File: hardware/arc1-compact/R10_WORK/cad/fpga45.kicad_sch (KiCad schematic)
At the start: 109 parts, among them J9 45F JTAG, U26 LFE5U-45F-6BG381C, U27 iso FPGA45_SCK_B, U28 iso FPGA45_MOSI, U29 iso FPGA45_SS_N, X1 125MHz, X2 25MHz

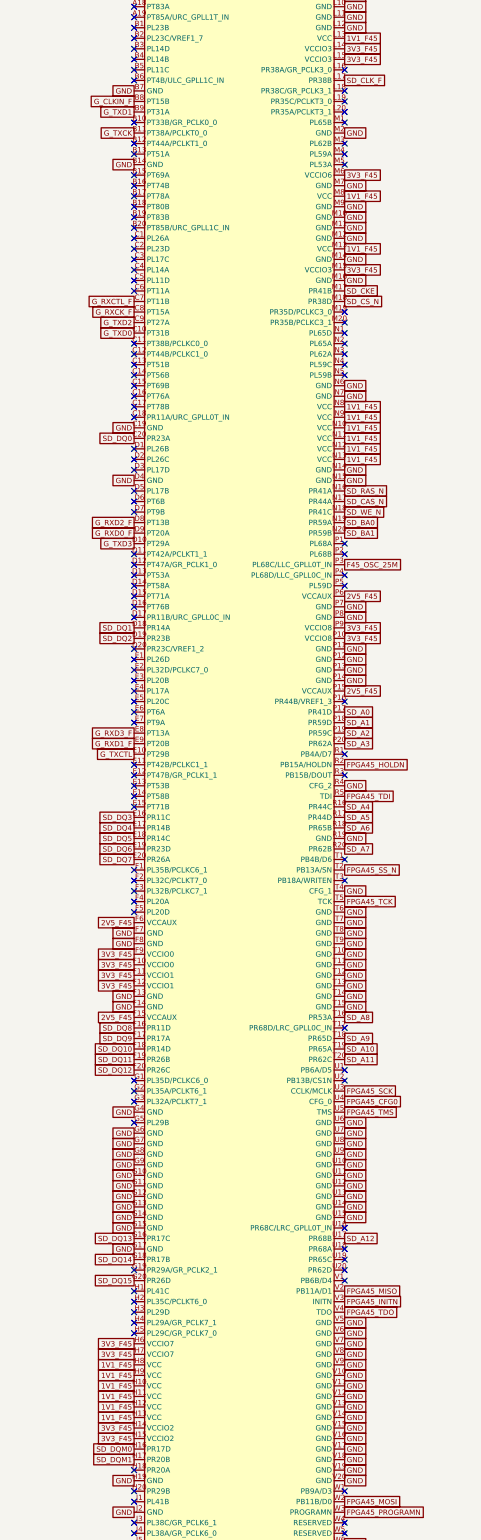
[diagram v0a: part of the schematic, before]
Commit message: R10 schematic: SDRAM net rename (collision with microSD clock found by crosscheck), 12F config buffers on 3V3_F12, crosscheck_r10 (A-H) PASS, every-pin review tables
Co-Authored-By: Claude Opus 5.5 <noreply@anthropic.com>
Claude-Session: https://claude.ai/code/session_01UkiuLdbjDvK75uDzAPKsGs
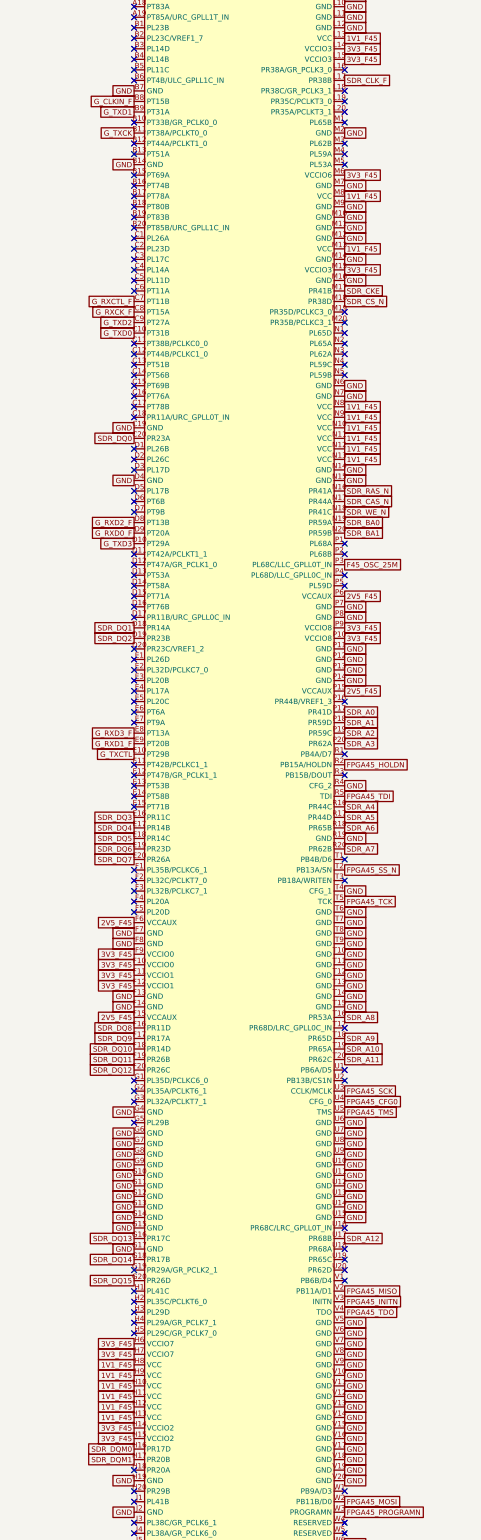
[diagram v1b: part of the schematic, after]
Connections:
- net SD_A0 renamed SDR_A0
- net SD_A1 renamed SDR_A1
- net SD_A10 renamed SDR_A10
- net SD_A11 renamed SDR_A11
- net SD_A12 renamed SDR_A12
- net SD_A2 renamed SDR_A2
- net SD_A3 renamed SDR_A3
- net SD_A4 renamed SDR_A4
- net SD_A5 renamed SDR_A5
- net SD_A6 renamed SDR_A6
- net SD_A7 renamed SDR_A7
- net SD_A8 renamed SDR_A8
- net SD_A9 renamed SDR_A9
- net SD_BA0 renamed SDR_BA0
- net SD_BA1 renamed SDR_BA1
- net SD_CAS_N renamed SDR_CAS_N
- net SD_CKE renamed SDR_CKE
- net SD_CLK_F renamed SDR_CLK_F
- net SD_CS_N renamed SDR_CS_N
- net SD_DQ0 renamed SDR_DQ0
- net SD_DQ1 renamed SDR_DQ1
- net SD_DQ10 renamed SDR_DQ10
- net SD_DQ11 renamed SDR_DQ11
- net SD_DQ12 renamed SDR_DQ12
- net SD_DQ13 renamed SDR_DQ13
- net SD_DQ14 renamed SDR_DQ14
- net SD_DQ15 renamed SDR_DQ15
- net SD_DQ2 renamed SDR_DQ2
- net SD_DQ3 renamed SDR_DQ3
- net SD_DQ4 renamed SDR_DQ4
- net SD_DQ5 renamed SDR_DQ5
- net SD_DQ6 renamed SDR_DQ6
- net SD_DQ7 renamed SDR_DQ7
- net SD_DQ8 renamed SDR_DQ8
- net SD_DQ9 renamed SDR_DQ9
- net SD_DQM0 renamed SDR_DQM0
- net SD_DQM1 renamed SDR_DQM1
- net SD_RAS_N renamed SDR_RAS_N
- net SD_WE_N renamed SDR_WE_N

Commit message: R10 change order rev 1.1: HDMI audio (ADV7513), USB0 role mux + hub + 2x front USB-A, eMMC, buttonless board
Owner handoff ARC1_R10_Handoff rev 1.1 (spec/, SHA-256 recorded) implemented in the generated schematic:
- D8 ADV7513BSWZ replaces the TFP410 (supersedes D6): D213 RGB888 video, D213 I2C2 init,
  F133 I2S2 -> HDMI embedded audio; own 1.8 V buck + 3 filtered domains; R_EXT 887R.
  D[23:0] pin order verified from the datasheet glyph coordinates.
- D9 F133 USB0 -> TS3USB221A (default rear USB-C device/FEL) or USB2422 hub -> two
  TPS2051C-switched front USB-A ports; F133 USB1 remains the internal D213 link; the D213
  recovery USB-C becomes internal fixture pads.
- D10 Samsung KLMAG1JETD-B041 16 GB eMMC on F133 SMHC0 (CONDITIONAL: SMHC0 documented for SD).
- D11 no switches: fixture pad pairs; game buttons, microSD and speakers removed.
- crosscheck_r10 section I (handoff go/no-go: 4 exterior connectors, 0 switches, I2S wired
  to the HDMI transmitter, USB0/USB1 roles, eMMC wiring) PASS; ERC 0/0; pin review PASS.
Sources: ADV7513 DS Rev B (LCSC copy), ADI AN-1270, Linux adv7511 driver, USB2422
DS00001726A, TPS20xxC SLVSAU6I, Samsung eMMC DS (not committed: vendor-confidential mark).

Co-Authored-By: Claude Opus 5.5 <noreply@anthropic.com>
Claude-Session: https://claude.ai/code/session_01UkiuLdbjDvK75uDzAPKsGs
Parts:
- removed C117, C118, C119, C120, C121, C122, C123, C124, C125, C126, C127, C128, C129, C130, C131, C132, C133, C134, C135, C136: 100nF, Capacitor_SMD:C_0402_1005Metric, symbol ARC1_R10:C0402
- removed C137, C138: 10uF, Capacitor_SMD:C_0603_1608Metric, symbol ARC1_R10:C0603
- removed D4: 45F LED, LED_SMD:LED_0603_1608Metric, symbol ARC1_R10:LED
- removed J9: 45F JTAG, Connector_PinHeader_1.27mm:PinHeader_2x05_P1.27mm_Vertical_SMD, symbol ARC1_R10:HDR_2x5_127
- removed R87, R88, R89, R90, R91, R92: 22R, Resistor_SMD:R_0402_1005Metric, symbol ARC1_R10:R0402
- removed TP50: G_TXCK, TestPoint:TestPoint_Pad_D1.0mm, symbol ARC1_R10:TP
- removed TP51: G_RXCK, TestPoint:TestPoint_Pad_D1.0mm, symbol ARC1_R10:TP
- removed TP52: G_CLKIN, TestPoint:TestPoint_Pad_D1.0mm, symbol ARC1_R10:TP
- removed TP53: FPGA45_DONE, TestPoint:TestPoint_Pad_D1.0mm, symbol ARC1_R10:TP
- removed TP54: FPGA45_PROGRAMN, TestPoint:TestPoint_Pad_D1.0mm, symbol ARC1_R10:TP
- removed TP55: FPGA45_INITN, TestPoint:TestPoint_Pad_D1.0mm, symbol ARC1_R10:TP
- removed TP56: FPGA45_SCK, TestPoint:TestPoint_Pad_D1.0mm, symbol ARC1_R10:TP
- removed TP57: F45_OSC_25M, TestPoint:TestPoint_Pad_D1.0mm, symbol ARC1_R10:TP
- removed U26: LFE5U-45F-6BG381C, Package_BGA:Lattice_caBGA-381_17x17mm_Layout20x20_P0.8mm, symbol ARC1_R10:ECP5_45F_BG381
- removed U27: iso FPGA45_SCK_B, Package_TO_SOT_SMD:SOT-353_SC-70-5, symbol ARC1_R10:LVC1G125
- removed U28: iso FPGA45_MOSI, Package_TO_SOT_SMD:SOT-353_SC-70-5, symbol ARC1_R10:LVC1G125
- removed U29: iso FPGA45_SS_N, Package_TO_SOT_SMD:SOT-353_SC-70-5, symbol ARC1_R10:LVC1G125
- removed X1: 125MHz, Oscillator:Oscillator_SMD_Abracon_ASE-4Pin_3.2x2.5mm, symbol ARC1_R10:OSC_3225
- added C174, C175, C176, C177, C178, C179, C180, C181, C182, C183, C184, C192, C193, C194, C195: 100nF, Capacitor_SMD:C_0402_1005Metric, symbol ARC1_R10:C0402
- added C185, C186, C187, C188, C189, C190, C191: 10uF, Capacitor_SMD:C_0603_1608Metric, symbol ARC1_R10:C0603
- added D5: 45F LED, LED_SMD:LED_0603_1608Metric, symbol ARC1_R10:LED
- added J15: 45F JTAG, Connector_PinHeader_1.27mm:PinHeader_2x05_P1.27mm_Vertical_SMD, symbol ARC1_R10:HDR_2x5_127
- added R123, R124, R125, R126: 4.7k, Resistor_SMD:R_0402_1005Metric, symbol ARC1_R10:R0402
- added R127: 33R, Resistor_SMD:R_0402_1005Metric, symbol ARC1_R10:R0402
- added R128: 1k, Resistor_SMD:R_0402_1005Metric, symbol ARC1_R10:R0402
- added TP58: G_TXCK, TestPoint:TestPoint_Pad_D1.0mm, symbol ARC1_R10:TP
- added TP59: G_RXCK, TestPoint:TestPoint_Pad_D1.0mm, symbol ARC1_R10:TP
- added TP60: G_CLKIN, TestPoint:TestPoint_Pad_D1.0mm, symbol ARC1_R10:TP
- added TP61: FPGA45_DONE, TestPoint:TestPoint_Pad_D1.0mm, symbol ARC1_R10:TP
- added TP62: FPGA45_PROGRAMN, TestPoint:TestPoint_Pad_D1.0mm, symbol ARC1_R10:TP
- added TP63: FPGA45_INITN, TestPoint:TestPoint_Pad_D1.0mm, symbol ARC1_R10:TP
- added TP64: FPGA45_SCK, TestPoint:TestPoint_Pad_D1.0mm, symbol ARC1_R10:TP
- added TP65: F45_OSC_25M, TestPoint:TestPoint_Pad_D1.0mm, symbol ARC1_R10:TP
- added U33: LFE5U-45F-6BG381C, Package_BGA:Lattice_caBGA-381_17x17mm_Layout20x20_P0.8mm, symbol ARC1_R10:ECP5_45F_BG381
- added U34: iso FPGA45_SCK_B, Package_TO_SOT_SMD:SOT-353_SC-70-5, symbol ARC1_R10:LVC1G125
- added U35: iso FPGA45_MOSI, Package_TO_SOT_SMD:SOT-353_SC-70-5, symbol ARC1_R10:LVC1G125
- added U36: iso FPGA45_SS_N, Package_TO_SOT_SMD:SOT-353_SC-70-5, symbol ARC1_R10:LVC1G125
- added X3: 25MHz, Oscillator:Oscillator_SMD_Abracon_ASE-4Pin_3.2x2.5mm, symbol ARC1_R10:OSC_3225
- C139, C144: value 10uF -> 100nF; footprint Capacitor_SMD:C_0603_1608Metric -> Capacitor_SMD:C_0402_1005Metric; symbol ARC1_R10:C0603 -> ARC1_R10:C0402; LCSC C19702 -> C1525; MPN CL10A106KP8NNNC -> CL05B104KO5NNNC
- C159, C160, C161: value 100nF -> 10uF; footprint Capacitor_SMD:C_0402_1005Metric -> Capacitor_SMD:C_0603_1608Metric; symbol ARC1_R10:C0402 -> ARC1_R10:C0603; LCSC C1525 -> C19702; MPN CL05B104KO5NNNC -> CL10A106KP8NNNC
- C163, C164, C165, C167, C168, C169: value 10uF -> 100nF; footprint Capacitor_SMD:C_0603_1608Metric -> Capacitor_SMD:C_0402_1005Metric; symbol ARC1_R10:C0603 -> ARC1_R10:C0402; LCSC C19702 -> C1525; MPN CL10A106KP8NNNC -> CL05B104KO5NNNC; Note one per VCCIO bank -> (none)
- C166: Note one per VCCIO bank -> (none)
- R100: value 100k -> 22R; LCSC C25741 -> C25092; MPN 0402WGF1003TCE -> 0402WGF220JTCE; Note 45F RX idle while the D213 PE7 is hi-Z -> 45F->D213 series R at the 45F (RXD0)
- R101: value 100k -> 22R; LCSC C25741 -> C25092; MPN 0402WGF1003TCE -> 0402WGF220JTCE; Note D213 GMAC RX idle while the 45F is off/unconfigured -> 45F->D213 series R at the 45F (RXD1)
- R102: value 0R -> 22R; LCSC C17168 -> C25092; MPN 0402WGF0000TCE -> 0402WGF220JTCE; Note D7 fallback: feed GMAC0_CLKIN from the 45F RGMII TX clock -> 45F->D213 series R at the 45F (RXD2); now fitted
- R103: value 0R -> 22R; LCSC C17168 -> C25092; MPN 0402WGF0000TCE -> 0402WGF220JTCE; Note D7 fallback oscillator link (DNP) -> 45F->D213 series R at the 45F (RXD3); now fitted
- R104: value 33R -> 22R; LCSC C25105 -> C25092; MPN 0402WGF330JTCE -> 0402WGF220JTCE; Note CCLK series 22-80R (TN-02038 Table 6.2) -> 45F->D213 series R at the 45F (RXCTL)
- R105: value 10k -> 22R; LCSC C25744 -> C25092; MPN 0402WGF1002TCE -> 0402WGF220JTCE; Note D213 side: deselected while the D213 is in reset -> 45F->D213 series R at the 45F (CLKIN)
- R106: Note (none) -> 45F RX idle while the D213 PE7 is hi-Z
- R107: Note (none) -> D213 GMAC RX idle while the 45F is off/unconfigured
- R108: value 100k -> 0R; LCSC C25741 -> C17168; MPN 0402WGF1003TCE -> 0402WGF0000TCE; Note defined at the D213 while the FPGA is off/unconfigured -> D7 fallback: feed GMAC0_CLKIN from the 45F RGMII TX clock; now not fitted
- R109: value 4.7k -> 0R; LCSC C25900 -> C17168; MPN 0402WGF4701TCE -> 0402WGF0000TCE; Note TN-02038: 4.7k to VCCIO8 -> D7 fallback oscillator link (DNP); now not fitted
- R110: value 470R -> 33R; LCSC (none) -> C25105; MPN (none) -> 0402WGF330JTCE; Manufacturer (none) -> UNI-ROYAL; Note D213 PA4 used open-drain (low or input) -> CCLK series 22-80R (TN-02038 Table 6.2); Reuse (none) -> SLIM4_R26_BOM_LINE (re-validate)
- R111: value 4.7k -> 10k; LCSC C25900 -> C25744; MPN 0402WGF4701TCE -> 0402WGF1002TCE; Note (none) -> D213 side: deselected while the D213 is in reset
- R112: value 4.7k -> 100k; LCSC C25900 -> C25741; MPN 0402WGF4701TCE -> 0402WGF1003TCE
- R113: value 4.7k -> 100k; LCSC C25900 -> C25741; MPN 0402WGF4701TCE -> 0402WGF1003TCE; Note SN pull-up (TN-02039 6.2) -> (none)
- R114: value 4.7k -> 100k; LCSC C25900 -> C25741; MPN 0402WGF4701TCE -> 0402WGF1003TCE; Note CFG[2:0] = 001 slave SPI -> defined at the D213 while the FPGA is off/unconfigured
- R115: value 10k -> 4.7k; LCSC C25744 -> C25900; MPN 0402WGF1002TCE -> 0402WGF4701TCE; Note (none) -> TN-02038: 4.7k to VCCIO8
- R116: value 1k -> 470R; LCSC C11702 -> (none); MPN 0402WGF1001TCE -> (none); Manufacturer UNI-ROYAL -> (none); Note CCLK 510R-1k pull-up -> D213 PA4 used open-drain (low or input); Reuse SLIM4_R26_BOM_LINE (re-validate) -> (none)
- R119: Note (none) -> SN pull-up (TN-02039 6.2)
- R120: Note (none) -> CFG[2:0] = 001 slave SPI
- R121: value 33R -> 10k; LCSC C25105 -> C25744; MPN 0402WGF330JTCE -> 0402WGF1002TCE
- R122: Note (none) -> CCLK 510R-1k pull-up
- R93: Note 45F->D213 series R at the 45F (RXCK) -> D213->45F series R at the D213 (TXCK)
- R94: Note 45F->D213 series R at the 45F (RXD0) -> D213->45F series R at the D213 (TXD0)
- R95: Note 45F->D213 series R at the 45F (RXD1) -> D213->45F series R at the D213 (TXD1)
- R96: Note 45F->D213 series R at the 45F (RXD2) -> D213->45F series R at the D213 (TXD2)
- R97: Note 45F->D213 series R at the 45F (RXD3) -> D213->45F series R at the D213 (TXD3)
- R98: Note 45F->D213 series R at the 45F (RXCTL) -> D213->45F series R at the D213 (TXCTL)
- R99: Note 45F->D213 series R at the 45F (CLKIN) -> 45F->D213 series R at the 45F (RXCK)
- X2: value 25MHz -> 125MHz; Note OE = VCC power-good: no clock into bank 6 before VCC and VC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 -> D7 fallback: independent 125 MHz MAC reference (DNP); now not fitted
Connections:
- net 1V1_F45: now also C140.1, C141.1, C142.1, C143.1, C144.1, C145.1, C146.1, C147.1, C148.1, C149.1, C150.1, C151.1, C152.1, C153.1, C154.1, C155.1, C156.1, C157.1, C158.1, C159.1, C160.1, C161.1, U33.H10 (VCC), U33.H11 (VCC), U33.H12 (VCC), U33.H13 (VCC), U33.H8 (VCC), U33.H9 (VCC), U33.J13 (VCC), U33.J8 (VCC), U33.K13 (VCC), U33.K8 (VCC), U33.L13 (VCC), U33.L8 (VCC), U33.M13 (VCC), U33.M8 (VCC), U33.N10 (VCC), U33.N11 (VCC), U33.N12 (VCC), U33.N13 (VCC), U33.N8 (VCC), U33.N9 (VCC)
- net 2V5_F45: now also C162.1, C163.1, C164.1, C165.1, C166.1, U33.F15 (VCCAUX), U33.F6 (VCCAUX), U33.P15 (VCCAUX), U33.P6 (VCCAUX); no longer C140.1, C141.1, C142.1, C143.1, C144.1
- net 3V3: now also R111.2, X2.1 (OE), X2.4 (VDD); no longer R105.2
- net 3V3_F45: now also R117.2, R121.2, R122.2, C174.1, C175.1, C176.1, C177.1, C178.1, C179.1, C180.1, C181.1, C182.1, C183.1, C184.1, C185.1, C186.1, C187.1, C188.1, C189.1, C190.1, C191.1, C192.1, C193.1, C194.1, C195.1, J15.1, R124.2, R125.2, R126.2, U33.F10 (VCCIO0), U33.F11 (VCCIO1), U33.F12 (VCCIO1), U33.F9 (VCCIO0), U33.H14 (VCCIO2), U33.H15 (VCCIO2), U33.H6 (VCCIO7), U33.H7 (VCCIO7), U33.J15 (VCCIO2), U33.J6 (VCCIO7), U33.L14 (VCCIO3), U33.L15 (VCCIO3), U33.L6 (VCCIO6), U33.L7 (VCCIO6), U33.M15 (VCCIO3), U33.M6 (VCCIO6), U33.P10 (VCCIO8), U33.P9 (VCCIO8), U34.5 (VCC), U35.5 (VCC), U36.5 (VCC), X3.4 (VDD); no longer C145.1, C146.1, C147.1, C148.1, C149.1, C150.1, C151.1, C152.1, C153.1, C154.1, C155.1, C156.1, C157.1, C158.1, C159.1, C160.1, C161.1, C162.1, C163.1, C164.1, C165.1, C166.1, R109.2, R111.2, R112.2, R113.2, R114.2, R116.2, X2.4 (VDD)
- net F45_LED0: now also R128.1, U33.A7 (PT18A); no longer R122.1
- net F45_LED0_R: now also D5.2 (A), R128.2; no longer R122.2
- net F45_OSC_25M: now also R127.2, TP65.1, U33.P3 (PL68C/LLC_GPLL0T_IN); no longer R121.2
- net F45_OSC_25M_X: now also R127.1, X3.3 (OUT); no longer R121.1, X2.3 (OUT)
- net FPGA45_CFG0: now also R120.1, U33.U4 (CFG_0); no longer R114.1
- net FPGA45_DONE: now also R118.1, TP61.1, U33.Y3 (DONE); no longer R112.1
- net FPGA45_HOLDN: now also R121.1, U33.R2 (PB15A/HOLDN); no longer R115.1
- net FPGA45_INITN: now also R117.1, TP63.1, U33.V3 (INITN); no longer R111.1
- net FPGA45_MISO: now also R114.1, U33.V2 (PB11A/D1); no longer R108.1
- net FPGA45_MOSI: now also U33.W2 (PB11B/D0), U35.4 (Y)
- net FPGA45_MOSI_D: now also R113.1, U35.2 (A); no longer R107.1
- net FPGA45_PROGRAMN: now also R115.1, R116.2, J15.10, TP62.1, U33.W3 (PROGRAMN); no longer R109.1, R110.2
- net FPGA45_PROGRAMN_D: now also R116.1; no longer R110.1
- net FPGA45_SCK: now also R110.2, R122.1, TP64.1, U33.U3 (CCLK/MCLK); no longer R104.2, R116.1
- net FPGA45_SCK_B: now also R110.1, U34.4 (Y); no longer R104.1
- net FPGA45_SCK_D: now also R112.1, U34.2 (A); no longer R106.1
- net FPGA45_SS_N: now also R119.1, U33.T2 (PB13A/SN), U36.4 (Y); no longer R113.1
- net FPGA45_SS_N_D: now also R111.1, U36.2 (A); no longer R105.1
- net FPGA45_TCK: now also J15.4, R123.1, U33.T5 (TCK); no longer R117.1
- net FPGA45_TDI: now also J15.8, R125.1, U33.R5 (TDI); no longer R119.1
- net FPGA45_TDO: now also J15.6, R126.1, U33.V4 (TDO); no longer R120.1
- net FPGA45_TMS: now also J15.2, R124.1, U33.U5 (TMS); no longer R118.1
- net FPGA45_VCC_PG: now also X3.1 (OE); no longer X2.1 (OE)
- net GND: now also R112.2, R113.2, R114.2, C174.2, C175.2, C176.2, C177.2, C178.2, C179.2, C180.2, C181.2, C182.2, C183.2, C184.2, C185.2, C186.2, C187.2, C188.2, C189.2, C190.2, C191.2, C192.2, C193.2, C194.2, C195.2, D5.1 (K), J15.3, J15.5, J15.9, R123.2, U33.B14 (GND), U33.B7 (GND), U33.C19 (GND), U33.D4 (GND), U33.F13 (GND), U33.F14 (GND), U33.F7 (GND), U33.F8 (GND), U33.G10 (GND), U33.G11 (GND), U33.G12 (GND), U33.G13 (GND), U33.G14 (GND), U33.G15 (GND), U33.G17 (GND), U33.G4 (GND), U33.G6 (GND), U33.G7 (GND), U33.G8 (GND), U33.G9 (GND), U33.H19 (GND), U33.J10 (GND), U33.J11 (GND), U33.J12 (GND), U33.J14 (GND), U33.J2 (GND), U33.J7 (GND), U33.J9 (GND), U33.K10 (GND), U33.K11 (GND), U33.K12 (GND), U33.K14 (GND), U33.K15 (GND), U33.K6 (GND), U33.K7 (GND), U33.K9 (GND), U33.L10 (GND), U33.L11 (GND), U33.L12 (GND), U33.L9 (GND), U33.M10 (GND), U33.M11 (GND), U33.M12 (GND), U33.M14 (GND), U33.M16 (GND), U33.M2 (GND), U33.M7 (GND), U33.M9 (GND), U33.N14 (GND), U33.N15 (GND), U33.N6 (GND), U33.N7 (GND), U33.P11 (GND), U33.P12 (GND), U33.P13 (GND), U33.P14 (GND), U33.P7 (GND), U33.P8 (GND), U33.R19 (GND), U33.R4 (CFG_2), U33.T10 (GND), U33.T11 (GND), U33.T12 (GND), U33.T13 (GND), U33.T14 (GND), U33.T15 (GND), U33.T4 (CFG_1), U33.T6 (GND), U33.T7 (GND), U33.T8 (GND), U33.T9 (GND), U33.U10 (GND), U33.U11 (GND), U33.U12 (GND), U33.U13 (GND), U33.U14 (GND), U33.U15 (GND), U33.U6 (GND), U33.U7 (GND), U33.U8 (GND), U33.U9 (GND), U33.V10 (GND), U33.V11 (GND), U33.V12 (GND), U33.V13 (GND), U33.V14 (GND), U33.V15 (GND), U33.V16 (GND), U33.V17 (GND), U33.V18 (GND), U33.V19 (GND), U33.V20 (GND), U33.V5 (GND), U33.V6 (GND), U33.V7 (GND), U33.V8 (GND), U33.V9 (GND), U33.W12 (GND), U33.W15 (GND), U33.W16 (GND), U33.W19 (GND), U33.W20 (GND), U33.W6 (GND), U33.W7 (GND), U33.Y11 (GND), U33.Y12 (GND), U33.Y14 (GND), U33.Y15 (GND), U33.Y16 (GND), U33.Y17 (GND), U33.Y19 (GND), U33.Y5 (GND), U33.Y6 (GND), U33.Y7 (GND), U33.Y8 (GND), U34.1 (~{OE}), U34.3 (GND), U35.1 (~{OE}), U35.3 (GND), U36.1 (~{OE}), U36.3 (GND), X3.2 (GND); no longer R100.2, R101.2, R108.2, R117.2
- net G_CLKIN: now also R105.2, R108.2, R109.2, TP60.1; no longer R102.2, R103.2, R99.2
- net G_CLKIN_F: now also R105.1, U33.B8 (PT15B); no longer R99.1
- net G_CLKIN_OSC: now also R109.1, X2.3 (OUT); no longer R103.1
- net G_RXCK: now also R108.1, R99.2, TP59.1; no longer R102.1, R93.2
- net G_RXCK_F: now also R99.1, U33.C8 (PT15A); no longer R93.1
- net G_RXCTL: now also R104.2, R107.1; no longer R101.1, R98.2
- net G_RXCTL_F: now also R104.1, U33.C7 (PT11B); no longer R98.1
- net G_RXD0: now also R100.2; no longer R94.2
- net G_RXD0_F: now also R100.1, U33.D9 (PT20A); no longer R94.1
- net G_RXD1: now also R101.2; no longer R95.2
- net G_RXD1_F: now also R101.1, U33.E9 (PT20B); no longer R95.1
- net G_RXD2: now also R102.2; no longer R96.2
- net G_RXD2_F: now also R102.1, U33.D8 (PT13B); no longer R96.1
- net G_RXD3: now also R103.2; no longer R97.2
- net G_RXD3_F: now also R103.1, U33.E8 (PT13A); no longer R97.1
- net G_TXCK: now also R93.2, TP58.1, U33.B11 (PT38A/PCLKT0_0)
- net G_TXCK_D: now also R93.1
- net G_TXCTL: now also R106.1, R98.2, U33.E10 (PT29B); no longer R100.1
- net G_TXCTL_D: now also R98.1
- net G_TXD0: now also R94.2, U33.C10 (PT31B)
- net G_TXD0_D: now also R94.1
- net G_TXD1: now also R95.2, U33.B9 (PT31A)
- net G_TXD1_D: now also R95.1
- net G_TXD2: now also R96.2, U33.C9 (PT27A)
- net G_TXD2_D: now also R96.1
- net G_TXD3: now also R97.2, U33.D10 (PT29A)
- net G_TXD3_D: now also R97.1
- net SDR_A0: now also U33.P17 (PR41D)
- net SDR_A1: now also U33.P18 (PR59D)
- net SDR_A10: now also U33.T19 (PR65A)
- net SDR_A11: now also U33.T20 (PR62C)
- net SDR_A12: now also U33.U17 (PR68B)
- net SDR_A2: now also U33.P19 (PR59C)
- net SDR_A3: now also U33.P20 (PR62A)
- net SDR_A4: now also U33.R16 (PR44C)
- net SDR_A5: now also U33.R17 (PR44D)
- net SDR_A6: now also U33.R18 (PR65B)
- net SDR_A7: now also U33.R20 (PR62B)
- net SDR_A8: now also U33.T16 (PR53A)
- net SDR_A9: now also U33.T18 (PR65D)
- net SDR_BA0: now also U33.N19 (PR59A)
- net SDR_BA1: now also U33.N20 (PR59B)
- net SDR_CAS_N: now also U33.N17 (PR44A)
- net SDR_CKE: now also U33.M17 (PR41B)
- net SDR_CLK_F: now also U33.L17 (PR38B)
- net SDR_CS_N: now also U33.M18 (PR38D)
- net SDR_DQ0: now also U33.C20 (PR23A)
- net SDR_DQ1: now also U33.D18 (PR14A)
- net SDR_DQ10: now also U33.F18 (PR14D)
- net SDR_DQ11: now also U33.F19 (PR26B)
- net SDR_DQ12: now also U33.F20 (PR26C)
- net SDR_DQ13: now also U33.G16 (PR17C)
- net SDR_DQ14: now also U33.G18 (PR17B)
- net SDR_DQ15: now also U33.G20 (PR26D)
- net SDR_DQ2: now also U33.D19 (PR23B)
- net SDR_DQ3: now also U33.E16 (PR11C)
- net SDR_DQ4: now also U33.E17 (PR14B)
- net SDR_DQ5: now also U33.E18 (PR14C)
- net SDR_DQ6: now also U33.E19 (PR23D)
- net SDR_DQ7: now also U33.E20 (PR26A)
- net SDR_DQ8: now also U33.F16 (PR11D)
- net SDR_DQ9: now also U33.F17 (PR17A)
- net SDR_DQM0: now also U33.H16 (PR17D)
- net SDR_DQM1: now also U33.H17 (PR20B)
- net SDR_RAS_N: now also U33.N16 (PR41A)
- net SDR_WE_N: now also U33.N18 (PR41C)
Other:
- moved on the sheet: C139, C140, C141, C142, C143, C144, C145, C146, C147, C148, C149, C150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

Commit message: R10 D12: top USB-A game cartridge, no eMMC; USB2514B 4-port hub (3 ports used)
Owner direction: games are played directly from a USB drive in a top USB-A "cartridge"
port; the two front USB-A ports are controller inputs; eMMC not needed.
- Schematic: eMMC sheet removed (F133 PF0-PF6 freed); USB2422 replaced by USB2514B-I/M2
  (strap mode CFG_SEL=00, port 4 disabled by strap, CRFILT/PLLFILT 0.1 uF per DS00001692C);
  third TPS2051C + ESD + TVS + vertical USB-A (Molex 105057) marked TOP.
- crosscheck I: five exterior connectors (rear USB-C + HDMI, 2x front USB-A, top USB-A),
  eMMC/USB2422 must be absent, all three ports on the hub. PASS. ERC 0/0, pin review and
  pin/function matrix PASS, R10_HOST_CHECKS_PASS.
- PCB regenerated: Ø 119.8 mm, DRC 0 errors (unrouted), top cartridge at (-9.3, 24.2) mm.
- DECISIONS D12 (supersedes D10 and the four-connector rule); change-order report sections
  1, 2, 4, 5, 6 and the mechanical note updated; CLAUDE.md topology line amended.

Co-Authored-By: Claude Opus 5.5 <noreply@anthropic.com>
Claude-Session: https://claude.ai/code/session_01UkiuLdbjDvK75uDzAPKsGs
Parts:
- removed C139, C140, C141, C142, C143, C144, C145, C146: 100nF, Capacitor_SMD:C_0402_1005Metric, symbol ARC1_R10:C0402
- removed D5: 45F LED, LED_SMD:LED_0603_1608Metric, symbol ARC1_R10:LED
- removed J15: 45F JTAG, Connector_PinHeader_1.27mm:PinHeader_2x05_P1.27mm_Vertical_SMD, symbol ARC1_R10:HDR_2x5_127
- removed R93, R94, R95, R96, R97: 22R, Resistor_SMD:R_0402_1005Metric, symbol ARC1_R10:R0402
- removed TP58: G_TXCK, TestPoint:TestPoint_Pad_D1.0mm, symbol ARC1_R10:TP
- removed U33: LFE5U-45F-6BG381C, Package_BGA:Lattice_caBGA-381_17x17mm_Layout20x20_P0.8mm, symbol ARC1_R10:ECP5_45F_BG381
- removed U34: iso FPGA45_SCK_B, Package_TO_SOT_SMD:SOT-353_SC-70-5, symbol ARC1_R10:LVC1G125
- added C196, C197, C198, C199: 10uF, Capacitor_SMD:C_0603_1608Metric, symbol ARC1_R10:C0603
- added C200, C201, C202, C203: 100nF, Capacitor_SMD:C_0402_1005Metric, symbol ARC1_R10:C0402
- added D6: 45F LED, LED_SMD:LED_0603_1608Metric, symbol ARC1_R10:LED
- added J16: 45F JTAG, Connector_PinHeader_1.27mm:PinHeader_2x05_P1.27mm_Vertical_SMD, symbol ARC1_R10:HDR_2x5_127
- added R129, R130, R131: 4.7k, Resistor_SMD:R_0402_1005Metric, symbol ARC1_R10:R0402
- added R132: 33R, Resistor_SMD:R_0402_1005Metric, symbol ARC1_R10:R0402
- added R133: 1k, Resistor_SMD:R_0402_1005Metric, symbol ARC1_R10:R0402
- added TP66: F45_OSC_25M, TestPoint:TestPoint_Pad_D1.0mm, symbol ARC1_R10:TP
- added U37: iso FPGA45_MOSI, Package_TO_SOT_SMD:SOT-353_SC-70-5, symbol ARC1_R10:LVC1G125
- added U38: iso FPGA45_SS_N, Package_TO_SOT_SMD:SOT-353_SC-70-5, symbol ARC1_R10:LVC1G125
- C159, C160, C161, C166: value 10uF -> 100nF; footprint Capacitor_SMD:C_0603_1608Metric -> Capacitor_SMD:C_0402_1005Metric; symbol ARC1_R10:C0603 -> ARC1_R10:C0402; LCSC C19702 -> C1525; MPN CL10A106KP8NNNC -> CL05B104KO5NNNC
- C167, C168, C169, C174: value 100nF -> 10uF; footprint Capacitor_SMD:C_0402_1005Metric -> Capacitor_SMD:C_0603_1608Metric; symbol ARC1_R10:C0402 -> ARC1_R10:C0603; LCSC C1525 -> C19702; MPN CL05B104KO5NNNC -> CL10A106KP8NNNC
- C185, C186, C187, C188, C189, C190, C191: value 10uF -> 100nF; footprint Capacitor_SMD:C_0603_1608Metric -> Capacitor_SMD:C_0402_1005Metric; symbol ARC1_R10:C0603 -> ARC1_R10:C0402; LCSC C19702 -> C1525; MPN CL10A106KP8NNNC -> CL05B104KO5NNNC; Note one per VCCIO bank -> (none)
- C193, C194, C195: value 100nF -> 10uF; footprint Capacitor_SMD:C_0402_1005Metric -> Capacitor_SMD:C_0603_1608Metric; symbol ARC1_R10:C0402 -> ARC1_R10:C0603; LCSC C1525 -> C19702; MPN CL05B104KO5NNNC -> CL10A106KP8NNNC; Note (none) -> one per VCCIO bank
- R100: Note 45F->D213 series R at the 45F (RXD0) -> D213->45F series R at the D213 (TXD1)
- R101: Note 45F->D213 series R at the 45F (RXD1) -> D213->45F series R at the D213 (TXD2)
- R102: Note 45F->D213 series R at the 45F (RXD2) -> D213->45F series R at the D213 (TXD3)
- R103: Note 45F->D213 series R at the 45F (RXD3) -> D213->45F series R at the D213 (TXCTL)
- R104: Note 45F->D213 series R at the 45F (RXCTL) -> 45F->D213 series R at the 45F (RXCK)
- R105: Note 45F->D213 series R at the 45F (CLKIN) -> 45F->D213 series R at the 45F (RXD0)
- R106: value 100k -> 22R; LCSC C25741 -> C25092; MPN 0402WGF1003TCE -> 0402WGF220JTCE; Note 45F RX idle while the D213 PE7 is hi-Z -> 45F->D213 series R at the 45F (RXD1)
- R107: value 100k -> 22R; LCSC C25741 -> C25092; MPN 0402WGF1003TCE -> 0402WGF220JTCE; Note D213 GMAC RX idle while the 45F is off/unconfigured -> 45F->D213 series R at the 45F (RXD2)
- R108: value 0R -> 22R; LCSC C17168 -> C25092; MPN 0402WGF0000TCE -> 0402WGF220JTCE; Note D7 fallback: feed GMAC0_CLKIN from the 45F RGMII TX clock -> 45F->D213 series R at the 45F (RXD3); now fitted
- R109: value 0R -> 22R; LCSC C17168 -> C25092; MPN 0402WGF0000TCE -> 0402WGF220JTCE; Note D7 fallback oscillator link (DNP) -> 45F->D213 series R at the 45F (RXCTL); now fitted
- R110: value 33R -> 22R; LCSC C25105 -> C25092; MPN 0402WGF330JTCE -> 0402WGF220JTCE; Note CCLK series 22-80R (TN-02038 Table 6.2) -> 45F->D213 series R at the 45F (CLKIN)
- R111: value 10k -> 100k; LCSC C25744 -> C25741; MPN 0402WGF1002TCE -> 0402WGF1003TCE; Note D213 side: deselected while the D213 is in reset -> 45F RX idle while the D213 PE7 is hi-Z
- R112: Note (none) -> D213 GMAC RX idle while the 45F is off/unconfigured
- R113: value 100k -> 0R; LCSC C25741 -> C17168; MPN 0402WGF1003TCE -> 0402WGF0000TCE; Note (none) -> D7 fallback: feed GMAC0_CLKIN from the 45F RGMII TX clock; now not fitted
- R114: value 100k -> 0R; LCSC C25741 -> C17168; MPN 0402WGF1003TCE -> 0402WGF0000TCE; Note defined at the D213 while the FPGA is off/unconfigured -> D7 fallback oscillator link (DNP); now not fitted
- R115: value 4.7k -> 33R; LCSC C25900 -> C25105; MPN 0402WGF4701TCE -> 0402WGF330JTCE; Note TN-02038: 4.7k to VCCIO8 -> CCLK series 22-80R (TN-02038 Table 6.2)
- R116: value 470R -> 10k; LCSC (none) -> C25744; MPN (none) -> 0402WGF1002TCE; Manufacturer (none) -> UNI-ROYAL; Note D213 PA4 used open-drain (low or input) -> D213 side: deselected while the D213 is in reset; Reuse (none) -> SLIM4_R26_BOM_LINE (re-validate)
- R117, R118: value 4.7k -> 100k; LCSC C25900 -> C25741; MPN 0402WGF4701TCE -> 0402WGF1003TCE
- R119: value 4.7k -> 100k; LCSC C25900 -> C25741; MPN 0402WGF4701TCE -> 0402WGF1003TCE; Note SN pull-up (TN-02039 6.2) -> defined at the D213 while the FPGA is off/unconfigured
- R120: Note CFG[2:0] = 001 slave SPI -> TN-02038: 4.7k to VCCIO8
- R121: value 10k -> 470R; LCSC C25744 -> (none); MPN 0402WGF1002TCE -> (none); Manufacturer UNI-ROYAL -> (none); Note (none) -> D213 PA4 used open-drain (low or input); Reuse SLIM4_R26_BOM_LINE (re-validate) -> (none)
- R122: value 1k -> 4.7k; LCSC C11702 -> C25900; MPN 0402WGF1001TCE -> 0402WGF4701TCE; Note CCLK 510R-1k pull-up -> (none)
- R124: Note (none) -> SN pull-up (TN-02039 6.2)
- R125: Note (none) -> CFG[2:0] = 001 slave SPI
- R126: value 4.7k -> 10k; LCSC C25900 -> C25744; MPN 0402WGF4701TCE -> 0402WGF1002TCE
- R127: value 33R -> 1k; LCSC C25105 -> C11702; MPN 0402WGF330JTCE -> 0402WGF1001TCE; Note (none) -> CCLK 510R-1k pull-up
- R128: value 1k -> 4.7k; LCSC C11702 -> C25900; MPN 0402WGF1001TCE -> 0402WGF4701TCE
- R98: Note D213->45F series R at the D213 (TXCTL) -> D213->45F series R at the D213 (TXCK)
- R99: Note 45F->D213 series R at the 45F (RXCK) -> D213->45F series R at the D213 (TXD0)
- TP59: value G_RXCK -> G_TXCK
- TP60: value G_CLKIN -> G_RXCK
- TP61: value FPGA45_DONE -> G_CLKIN
- TP62: value FPGA45_PROGRAMN -> FPGA45_DONE
- TP63: value FPGA45_INITN -> FPGA45_PROGRAMN
- TP64: value FPGA45_SCK -> FPGA45_INITN
- TP65: value F45_OSC_25M -> FPGA45_SCK
- U35: value iso FPGA45_MOSI -> LFE5U-45F-6BG381C; footprint Package_TO_SOT_SMD:SOT-353_SC-70-5 -> Package_BGA:Lattice_caBGA-381_17x17mm_Layout20x20_P0.8mm; symbol ARC1_R10:LVC1G125 -> ARC1_R10:ECP5_45F_BG381; MPN SN74LVC1G125DCKR -> LFE5U-45F-6BG381C; Manufacturer Texas Instruments -> Lattice; Note Ioff: no current into the FPGA rail while 3V3_F45 is off -> (none); Source SN74LVC1G125 DS pin functions (sources/glue) -> Lattice FPGA-DS-02012 v3.4 + pinout FPGA-SC-02034 (sources/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
- U36: value iso FPGA45_SS_N -> iso FPGA45_SCK_B
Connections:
- net 1V1_F45: now also C162.1, C163.1, C164.1, C165.1, C166.1, C167.1, C168.1, C169.1, U35.H10 (VCC), U35.H11 (VCC), U35.H12 (VCC), U35.H13 (VCC), U35.H8 (VCC), U35.H9 (VCC), U35.J13 (VCC), U35.J8 (VCC), U35.K13 (VCC), U35.K8 (VCC), U35.L13 (VCC), U35.L8 (VCC), U35.M13 (VCC), U35.M8 (VCC), U35.N10 (VCC), U35.N11 (VCC), U35.N12 (VCC), U35.N13 (VCC), U35.N8 (VCC), U35.N9 (VCC)
- net 2V5_F45: now also C170.1, C171.1, C172.1, C173.1, C174.1, U35.F15 (VCCAUX), U35.F6 (VCCAUX), U35.P15 (VCCAUX), U35.P6 (VCCAUX); no longer C162.1, C163.1, C164.1, C165.1, C166.1
- net 3V3: now also R116.2; no longer R111.2
- net 3V3_F45: now also R123.2, R127.2, U35.F10 (VCCIO0), U35.F11 (VCCIO1), U35.F12 (VCCIO1), U35.F9 (VCCIO0), U35.H14 (VCCIO2), U35.H15 (VCCIO2), U35.H6 (VCCIO7), U35.H7 (VCCIO7), U35.J15 (VCCIO2), U35.J6 (VCCIO7), U35.L14 (VCCIO3), U35.L15 (VCCIO3), U35.L6 (VCCIO6), U35.L7 (VCCIO6), U35.M15 (VCCIO3), U35.M6 (VCCIO6), U35.P10 (VCCIO8), U35.P9 (VCCIO8), C196.1, C197.1, C198.1, C199.1, C200.1, C201.1, C202.1, C203.1, J16.1, R129.2, R130.2, R131.2, U37.5 (VCC), U38.5 (VCC); no longer C167.1, C168.1, C169.1, C170.1, C171.1, C172.1, C173.1, C174.1, R115.2, R117.2, R118.2, R119.2, R121.2, U35.5 (VCC)
- net F45_LED0: now also U35.A7 (PT18A), R133.1; no longer R128.1
- net F45_LED0_R: now also D6.2 (A), R133.2; no longer R128.2
- net F45_OSC_25M: now also U35.P3 (PL68C/LLC_GPLL0T_IN), R132.2, TP66.1; no longer R127.2, TP65.1
- net F45_OSC_25M_X: now also R132.1; no longer R127.1
- net FPGA45_CFG0: now also R125.1, U35.U4 (CFG_0); no longer R120.1
- net FPGA45_DONE: now also R123.1, TP62.1, U35.Y3 (DONE); no longer R118.1, TP61.1
- net FPGA45_HOLDN: now also R126.1, U35.R2 (PB15A/HOLDN); no longer R121.1
- net FPGA45_INITN: now also R122.1, TP64.1, U35.V3 (INITN); no longer R117.1, TP63.1
- net FPGA45_MISO: now also R119.1, U35.V2 (PB11A/D1); no longer R114.1
- net FPGA45_MOSI: now also U35.W2 (PB11B/D0), U37.4 (Y); no longer U35.4 (Y)
- net FPGA45_MOSI_D: now also R118.1, U37.2 (A); no longer R113.1, U35.2 (A)
- net FPGA45_PROGRAMN: now also R120.1, R121.2, TP63.1, U35.W3 (PROGRAMN), J16.10; no longer R115.1, R116.2, TP62.1
- net FPGA45_PROGRAMN_D: now also R121.1; no longer R116.1
- net FPGA45_SCK: now also R115.2, R127.1, TP65.1, U35.U3 (CCLK/MCLK); no longer R110.2, R122.1, TP64.1
- net FPGA45_SCK_B: now also R115.1, U36.4 (Y); no longer R110.1
- net FPGA45_SCK_D: now also R117.1, U36.2 (A); no longer R112.1
- net FPGA45_SS_N: now also R124.1, U35.T2 (PB13A/SN), U38.4 (Y); no longer R119.1, U36.4 (Y)
- net FPGA45_SS_N_D: now also R116.1, U38.2 (A); no longer R111.1, U36.2 (A)
- net FPGA45_TCK: now also R128.1, U35.T5 (TCK), J16.4; no longer R123.1
- net FPGA45_TDI: now also U35.R5 (TDI), J16.8, R130.1; no longer R125.1
- net FPGA45_TDO: now also U35.V4 (TDO), J16.6, R131.1; no longer R126.1
- net FPGA45_TMS: now also U35.U5 (TMS), J16.2, R129.1; no longer R124.1
- net GND: now also R111.2, R117.2, R118.2, R119.2, R128.2, U35.B14 (GND), U35.B7 (GND), U35.C19 (GND), U35.D4 (GND), U35.F13 (GND), U35.F14 (GND), U35.F7 (GND), U35.F8 (GND), U35.G10 (GND), U35.G11 (GND), U35.G12 (GND), U35.G13 (GND), U35.G14 (GND), U35.G15 (GND), U35.G17 (GND), U35.G4 (GND), U35.G6 (GND), U35.G7 (GND), U35.G8 (GND), U35.G9 (GND), U35.H19 (GND), U35.J10 (GND), U35.J11 (GND), U35.J12 (GND), U35.J14 (GND), U35.J2 (GND), U35.J7 (GND), U35.J9 (GND), U35.K10 (GND), U35.K11 (GND), U35.K12 (GND), U35.K14 (GND), U35.K15 (GND), U35.K6 (GND), U35.K7 (GND), U35.K9 (GND), U35.L10 (GND), U35.L11 (GND), U35.L12 (GND), U35.L9 (GND), U35.M10 (GND), U35.M11 (GND), U35.M12 (GND), U35.M14 (GND), U35.M16 (GND), U35.M2 (GND), U35.M7 (GND), U35.M9 (GND), U35.N14 (GND), U35.N15 (GND), U35.N6 (GND), U35.N7 (GND), U35.P11 (GND), U35.P12 (GND), U35.P13 (GND), U35.P14 (GND), U35.P7 (GND), U35.P8 (GND), U35.R19 (GND), U35.R4 (CFG_2), U35.T10 (GND), U35.T11 (GND), U35.T12 (GND), U35.T13 (GND), U35.T14 (GND), U35.T15 (GND), U35.T4 (CFG_1), U35.T6 (GND), U35.T7 (GND), U35.T8 (GND), U35.T9 (GND), U35.U10 (GND), U35.U11 (GND), U35.U12 (GND), U35.U13 (GND), U35.U14 (GND), U35.U15 (GND), U35.U6 (GND), U35.U7 (GND), U35.U8 (GND), U35.U9 (GND), U35.V10 (GND), U35.V11 (GND), U35.V12 (GND), U35.V13 (GND), U35.V14 (GND), U35.V15 (GND), U35.V16 (GND), U35.V17 (GND), U35.V18 (GND), U35.V19 (GND), U35.V20 (GND), U35.V5 (GND), U35.V6 (GND), U35.V7 (GND), U35.V8 (GND), U35.V9 (GND), U35.W12 (GND), U35.W15 (GND), U35.W16 (GND), U35.W19 (GND), U35.W20 (GND), U35.W6 (GND), U35.W7 (GND), U35.Y11 (GND), U35.Y12 (GND), U35.Y14 (GND), U35.Y15 (GND), U35.Y16 (GND), U35.Y17 (GND), U35.Y19 (GND), U35.Y5 (GND), U35.Y6 (GND), U35.Y7 (GND), U35.Y8 (GND), C196.2, C197.2, C198.2, C199.2, C200.2, C201.2, C202.2, C203.2, D6.1 (K), J16.3, J16.5, J16.9, U37.1 (~{OE}), U37.3 (GND), U38.1 (~{OE}), U38.3 (GND); no longer R106.2, R107.2, R113.2, R114.2, R123.2, U35.1 (~{OE}), U35.3 (GND)
- net G_CLKIN: now also R110.2, R113.2, R114.2, TP61.1; no longer R105.2, R108.2, R109.2, TP60.1
- net G_CLKIN_F: now also R110.1, U35.B8 (PT15B); no longer R105.1
- net G_CLKIN_OSC: now also R114.1; no longer R109.1
- net G_RXCK: now also R104.2, R113.1, TP60.1; no longer R108.1, R99.2, TP59.1
- net G_RXCK_F: now also R104.1, U35.C8 (PT15A); no longer R99.1
- net G_RXCTL: now also R109.2, R112.1; no longer R104.2, R107.1
- net G_RXCTL_F: now also R109.1, U35.C7 (PT11B); no longer R104.1
- net G_RXD0: now also R105.2; no longer R100.2
- net G_RXD0_F: now also R105.1, U35.D9 (PT20A); no longer R100.1
- net G_RXD1: now also R106.2; no longer R101.2
- net G_RXD1_F: now also R106.1, U35.E9 (PT20B); no longer R101.1
- net G_RXD2: now also R107.2; no longer R102.2
- net G_RXD2_F: now also R107.1, U35.D8 (PT13B); no longer R102.1
- net G_RXD3: now also R108.2; no longer R103.2
- net G_RXD3_F: now also R108.1, U35.E8 (PT13A); no longer R103.1
- net G_TXCK: now also R98.2, TP59.1, U35.B11 (PT38A/PCLKT0_0)
- net G_TXCK_D: now also R98.1
- net G_TXCTL: now also R103.2, R111.1, U35.E10 (PT29B); no longer R106.1, R98.2
- net G_TXCTL_D: now also R103.1; no longer R98.1
- net G_TXD0: now also R99.2, U35.C10 (PT31B)
- net G_TXD0_D: now also R99.1
- net G_TXD1: now also R100.2, U35.B9 (PT31A)
- net G_TXD1_D: now also R100.1
- net G_TXD2: now also R101.2, U35.C9 (PT27A)
- net G_TXD2_D: now also R101.1
- net G_TXD3: now also R102.2, U35.D10 (PT29A)
- net G_TXD3_D: now also R102.1
- net SDR_A0: now also U35.P17 (PR41D)
- net SDR_A1: now also U35.P18 (PR59D)
- net SDR_A10: now also U35.T19 (PR65A)
- net SDR_A11: now also U35.T20 (PR62C)
- net SDR_A12: now also U35.U17 (PR68B)
- net SDR_A2: now also U35.P19 (PR59C)
- net SDR_A3: now also U35.P20 (PR62A)
- net SDR_A4: now also U35.R16 (PR44C)
- net SDR_A5: now also U35.R17 (PR44D)
- net SDR_A6: now also U35.R18 (PR65B)
- net SDR_A7: now also U35.R20 (PR62B)
- net SDR_A8: now also U35.T16 (PR53A)
- net SDR_A9: now also U35.T18 (PR65D)
- net SDR_BA0: now also U35.N19 (PR59A)
- net SDR_BA1: now also U35.N20 (PR59B)
- net SDR_CAS_N: now also U35.N17 (PR44A)
- net SDR_CKE: now also U35.M17 (PR41B)
- net SDR_CLK_F: now also U35.L17 (PR38B)
- net SDR_CS_N: now also U35.M18 (PR38D)
- net SDR_DQ0: now also U35.C20 (PR23A)
- net SDR_DQ1: now also U35.D18 (PR14A)
- net SDR_DQ10: now also U35.F18 (PR14D)
- net SDR_DQ11: now also U35.F19 (PR26B)
- net SDR_DQ12: now also U35.F20 (PR26C)
- net SDR_DQ13: now also U35.G16 (PR17C)
- net SDR_DQ14: now also U35.G18 (PR17B)
- net SDR_DQ15: now also U35.G20 (PR26D)
- net SDR_DQ2: now also U35.D19 (PR23B)
- net SDR_DQ3: now also U35.E16 (PR11C)
- net SDR_DQ4: now also U35.E17 (PR14B)
- net SDR_DQ5: now also U35.E18 (PR14C)
- net SDR_DQ6: now also U35.E19 (PR23D)
- net SDR_DQ7: now also U35.E20 (PR26A)
- net SDR_DQ8: now also U35.F16 (PR11D)
- net SDR_DQ9: now also U35.F17 (PR17A)
- net SDR_DQM0: now also U35.H16 (PR17D)
- net SDR_DQM1: now also U35.H17 (PR20B)
- net SDR_RAS_N: now also U35.N16 (PR41A)
- net SDR_WE_N: now also U35.N18 (PR41C)
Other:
- moved on the sheet: C147, C148, C149, C150, C151, C152, C153, C154, C155, C156, C157, C158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
